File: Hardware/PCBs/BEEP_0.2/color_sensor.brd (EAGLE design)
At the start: 26.2 x 44.7 mm, 19 parts, among them IC2 TCS32X0, IC3 TCS32X0, IC4 TCS32X0

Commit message: continue work on bottom pcbs
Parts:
- flipped JP1 to the bottom
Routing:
- net COLOR_SENSOR_2: track 54.7 -> 52.5 mm
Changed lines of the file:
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@@
 <element name="IC4" library="BEEP" package="TCS32X0" value="TCS32X0" x="13.97" y="16.51" rot="R180"/>
 <element name="C3" library="rcl" package="C0805" value="100n" x="8.9662" y="16.7386" rot="R270"/>
-<element name="JP1" library="pinhead" package="1X09" value="" x="23.0378" y="26.162" rot="R270"/>
+<element name="JP1" library="pinhead" package="1X09" value="" x="23.0378" y="26.162" rot="MR270"/>
 <element name="R1" library="rcl" package="M0805" value="" x="15.1638" y="7.2898" rot="R180"/>
 <element name="LED1" library="led" package="NFSG036BT" value="NFSG036BT" x="21.7424" y="7.9756" rot="R270"/>
@@
 <wire x1="9.5758" y1="42.5704" x2="9.5758" y2="45.1358" width="0.2032" layer="16"/>
 <via x="9.5758" y="45.1358" extent="1-16" drill="0.75" shape="octagon"/>
-<wire x1="23.0378" y1="36.322" x2="21.3614" y2="36.2712" width="0.2032" layer="1"/>
-<wire x1="21.3614" y1="36.2712" x2="17.2466" y2="40.386" width="0.2032" layer="1"/>
 <wire x1="17.2466" y1="40.386" x2="17.2466" y2="43.7134" width="0.2032" layer="1"/>
 <wire x1="17.2466" y1="43.7134" x2="15.7988" y2="45.1612" width="0.2032" layer="1"/>
@@
 <wire x1="6.604" y1="43.434" x2="4.6698" y2="43.434" width="0.2032" layer="1"/>
 <wire x1="4.6698" y1="43.434" x2="4.6482" y2="43.4556" width="0.2032" layer="1"/>
+<wire x1="23.0378" y1="36.322" x2="21.3106" y2="36.322" width="0.2032" layer="1"/>
+<wire x1="21.3106" y1="36.322" x2="17.2466" y2="40.386" width="0.2032" layer="1"/>
 <wire x1="9.2964" y1="29.8044" x2="10.011" y2="29.63" width="0" layer="19" extent="1-1"/>
 </signal>
@@
 <wire x1="12.1158" y1="38.3794" x2="12.1158" y2="37.0958" width="0.2032" layer="1"/>
 <wire x1="12.1158" y1="37.0958" x2="12.065" y2="37.045" width="0.2032" layer="1"/>
-<wire x1="23.0378" y1="33.782" x2="22.3012" y2="33.7312" width="0.2032" layer="1"/>
-<wire x1="22.3012" y1="33.7312" x2="15.9004" y2="40.132" width="0.2032" layer="1"/>
 <wire x1="15.9004" y1="40.132" x2="15.9004" y2="41.6696" width="0.2032" layer="1"/>
 <wire x1="15.9004" y1="41.6696" x2="15.875" y2="41.695" width="0.2032" layer="1"/>
 <wire x1="9.2964" y1="27.9044" x2="9.2964" y2="27.7486" width="0.2032" layer="1"/>
 <wire x1="9.2964" y1="27.7486" x2="12.065" y2="24.98" width="0.2032" layer="1"/>
+<wire x1="23.0378" y1="33.782" x2="22.2504" y2="33.782" width="0.2032" layer="1"/>
+<wire x1="22.2504" y1="33.782" x2="15.9004" y2="40.132" width="0.2032" layer="1"/>
 </signal>
 <signal name="COLOR_SENSOR_PWM_LED">
@@
 <contactref element="R2" pad="2"/>
 <contactref element="R3" pad="2"/>
-<wire x1="25.146" y1="32.131" x2="24.257" y2="31.242" width="0.2032" layer="1"/>
-<wire x1="24.257" y1="31.242" x2="23.0378" y2="31.242" width="0.2032" layer="1"/>
+<wire x1="25.146" y1="32.131" x2="24.511" y2="31.496" width="0.2032" layer="1"/>
 <wire x1="3.9624" y1="39.6596" x2="3.2106" y2="39.6596" width="0.2032" layer="1"/>
 <wire x1="3.2106" y1="39.6596" x2="2.54" y2="38.989" width="0.2032" layer="1"/>
@@
 <wire x1="12.954" y1="48.133" x2="2.794" y2="48.133" width="0.2032" layer="1"/>
 <wire x1="2.794" y1="48.133" x2="2.159" y2="47.498" width="0.2032" layer="1"/>
+<wire x1="23.0378" y1="31.242" x2="24.257" y2="31.242" width="0.2032" layer="1"/>
+<wire x1="24.257" y1="31.242" x2="24.511" y2="31.496" width="0.2032" layer="1"/>
 </signal>
 <signal name="COLOR_SENSOR_1">
@@
 <wire x1="2.921" y1="8.509" x2="3.429" y2="8.001" width="0.2032" layer="1"/>
 <wire x1="3.429" y1="8.001" x2="9.3472" y2="8.001" width="0.2032" layer="1"/>
-<wire x1="23.0378" y1="16.002" x2="23.0378" y2="11.7602" width="0.2032" layer="1"/>
 <wire x1="23.0378" y1="11.7602" x2="24.257" y2="10.541" width="0.2032" layer="1"/>
 <wire x1="24.257" y1="10.541" x2="24.257" y2="8.382" width="0.2032" layer="1"/>
@@
 <wire x1="18.923" y1="8.001" x2="18.288" y2="8.636" width="0.2032" layer="1"/>
 <wire x1="18.288" y1="8.636" x2="9.9822" y2="8.636" width="0.2032" layer="1"/>
+<wire x1="23.0378" y1="11.7602" x2="23.0378" y2="16.002" width="0.2032" layer="1"/>
 </signal>
 <signal name="COLOR_DIODE_1">
@@
 <wire x1="18.3134" y1="18.5928" x2="18.3134" y2="23.0886" width="0.2032" layer="16"/>
 <contactref element="JP1" pad="5"/>
-<wire x1="23.0378" y1="26.162" x2="20.9804" y2="26.1112" width="0.2032" layer="1"/>
-<wire x1="20.9804" y1="26.1112" x2="20.193" y2="26.8986" width="0.2032" layer="1"/>
 <wire x1="20.193" y1="26.8986" x2="20.193" y2="32.4104" width="0.2032" layer="1"/>
 <wire x1="20.193" y1="32.4104" x2="18.288" y2="34.3154" width="0.2032" layer="1"/>
+<wire x1="23.0378" y1="26.162" x2="20.9296" y2="26.162" width="0.2032" layer="1"/>
+<wire x1="20.9296" y1="26.162" x2="20.193" y2="26.8986" width="0.2032" layer="1"/>
 </signal>
 <signal name="COLOR_SENSOR_3">
@@
 <contactref element="JP1" pad="7"/>
 <wire x1="20.1676" y1="12.3444" x2="20.1676" y2="18.7452" width="0.2032" layer="1"/>
-<wire x1="20.1676" y1="18.7452" x2="22.4536" y2="21.0312" width="0.2032" layer="1"/>
-<wire x1="22.4536" y1="21.0312" x2="23.0378" y2="21.082" width="0.2032" layer="1"/>
 <wire x1="7.3914" y1="13.589" x2="7.3914" y2="18.8214" width="0.2032" layer="1"/>
 <wire x1="7.3914" y1="18.8214" x2="9.525" y2="20.955" width="0.2032" layer="1"/>
 <wire x1="9.525" y1="20.955" x2="12.3952" y2="20.955" width="0.2032" layer="1"/>
+<wire x1="23.0378" y1="21.082" x2="22.5044" y2="21.082" width="0.2032" layer="1"/>
+<wire x1="22.5044" y1="21.082" x2="20.1676" y2="18.7452" width="0.2032" layer="1"/>
 </signal>
 <signal name="COLOR_SENSOR_2">
@@
 <wire x1="19.1008" y1="10.16" x2="20.955" y2="12.0142" width="0.2032" layer="1"/>
 <wire x1="20.955" y1="12.0142" x2="20.955" y2="16.9926" width="0.2032" layer="1"/>
-<wire x1="20.955" y1="16.9926" x2="22.4028" y2="18.4404" width="0.2032" layer="1"/>
-<wire x1="22.4028" y1="18.4404" x2="24.1808" y2="18.4404" width="0.2032" layer="1"/>
-<wire x1="24.1808" y1="18.4404" x2="23.0378" y2="18.542" width="0.2032" layer="1"/>
 <wire x1="6.5532" y1="13.3096" x2="6.5532" y2="19.1262" width="0.2032" layer="1"/>
 <wire x1="6.5532" y1="19.1262" x2="8.89" y2="21.463" width="0.2032" layer="1"/>
@@
 <wire x1="11.557" y1="32.7914" x2="9.3726" y2="32.7914" width="0.2032" layer="1"/>
 <wire x1="9.3726" y1="32.7914" x2="6.985" y2="30.4038" width="0.2032" layer="1"/>
+<wire x1="23.0378" y1="18.542" x2="22.5044" y2="18.542" width="0.2032" layer="1"/>
+<wire x1="22.5044" y1="18.542" x2="20.955" y2="16.9926" width="0.2032" layer="1"/>
 </signal>
 <signal name="COLOR_FREQ_OUT">
@@
 <wire x1="18.288" y1="11.5824" x2="19.3548" y2="12.6492" width="0.2032" layer="1"/>
 <contactref element="JP1" pad="6"/>
-<wire x1="23.0378" y1="23.622" x2="21.8948" y2="23.622" width="0.2032" layer="1"/>
 <wire x1="21.8948" y1="23.622" x2="19.3548" y2="21.082" width="0.2032" layer="1"/>
 <wire x1="13.462" y1="23.495" x2="15.24" y2="21.717" width="0.2032" layer="1"/>
 <wire x1="15.24" y1="21.717" x2="18.8468" y2="21.717" width="0.2032" layer="1"/>
 <wire x1="18.8468" y1="21.717" x2="19.3548" y2="21.209" width="0.2032" layer="1"/>
+<wire x1="23.0378" y1="23.622" x2="21.8948" y2="23.622" width="0.2032" layer="1"/>
 </signal>
 <signal name="COLOR_DIODE_2">
@@
 <wire x1="16.7386" y1="24.2824" x2="17.1704" y2="24.7142" width="0.2032" layer="1"/>
 <contactref element="JP1" pad="4"/>
-<wire x1="23.0378" y1="28.702" x2="21.463" y2="28.6512" width="0.2032" layer="1"/>
-<wire x1="21.463" y1="28.6512" x2="20.8026" y2="29.3116" width="0.2032" layer="1"/>
 <wire x1="20.8026" y1="29.3116" x2="20.8026" y2="33.274" width="0.2032" layer="1"/>
 <wire x1="20.8026" y1="33.274" x2="18.5166" y2="35.56" width="0.2032" layer="1"/>
 <wire x1="18.5166" y1="35.56" x2="17.1958" y2="35.56" width="0.2032" layer="1"/>
 <wire x1="17.1958" y1="35.56" x2="17.145" y2="35.6108" width="0.2032" layer="1"/>
+<wire x1="23.0378" y1="28.702" x2="21.4122" y2="28.702" width="0.2032" layer="1"/>
+<wire x1="21.4122" y1="28.702" x2="20.8026" y2="29.3116" width="0.2032" layer="1"/>
 </signal>
 <signal name="N$1">

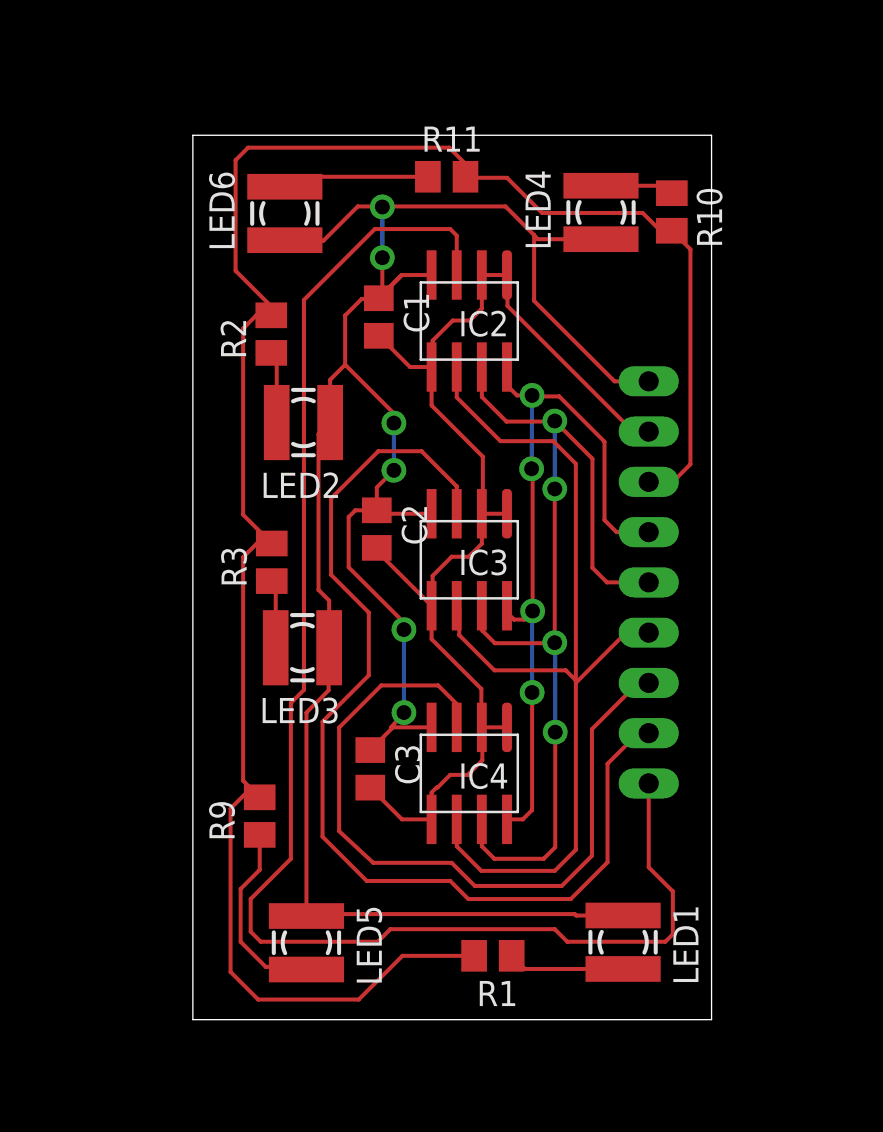
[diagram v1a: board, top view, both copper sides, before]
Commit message: the forgotten commit ;)
* enhance bottom, rgb sensor pcb
* create attiny and lm239 eval boards
* bug fix for the pdf export scripts
* correct attiny soft power switch simulation
* add experimental color sensor code
* add rgb color look up table
* correct motor roations
* various other (this is the forgetten commit)
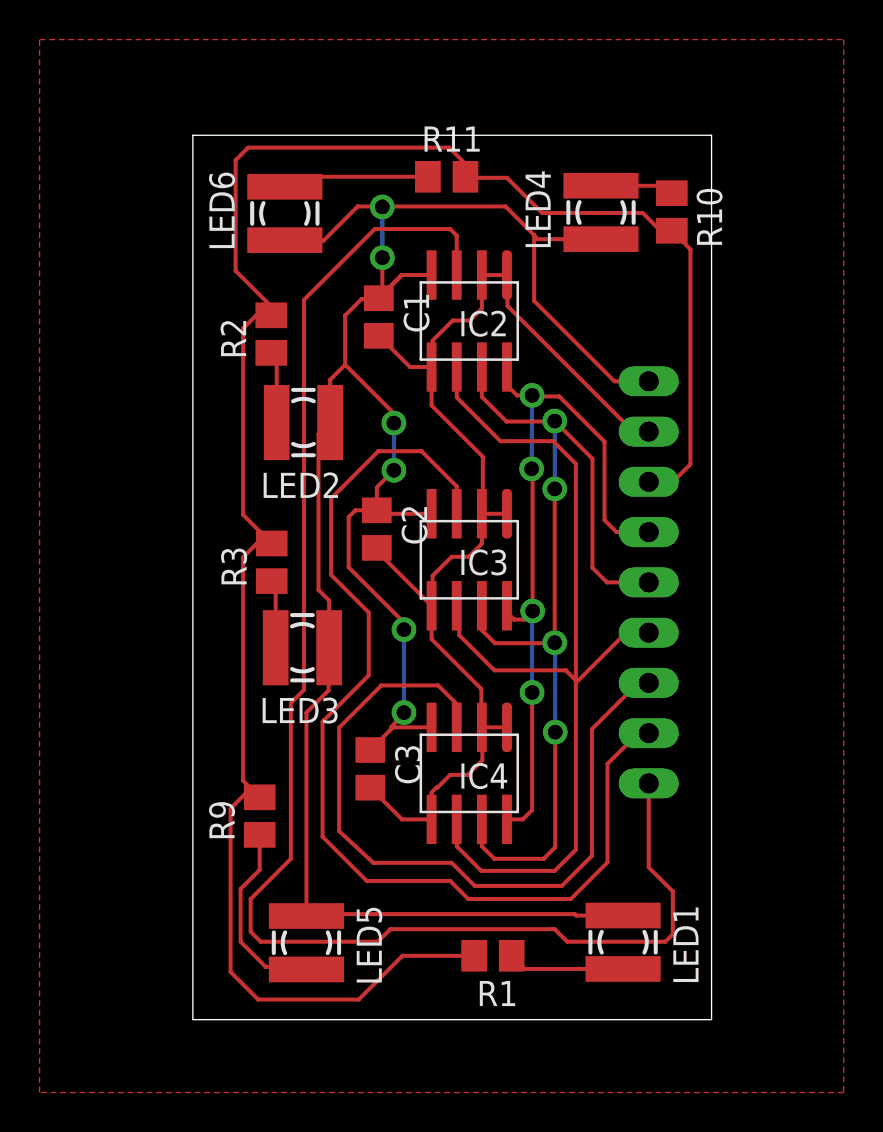
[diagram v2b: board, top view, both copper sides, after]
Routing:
- added copper zone on layer 1, net GND
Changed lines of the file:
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@@
 <layer number="43" name="vRestrict" color="2" fill="10" visible="yes" active="yes"/>
 <layer number="44" name="Drills" color="7" fill="1" visible="no" active="yes"/>
-<layer number="45" name="Holes" color="7" fill="1" visible="no" active="yes"/>
+<layer number="45" name="Holes" color="7" fill="1" visible="yes" active="yes"/>
 <layer number="46" name="Milling" color="3" fill="1" visible="no" active="yes"/>
 <layer number="47" name="Measures" color="7" fill="1" visible="no" active="yes"/>
-<layer number="48" name="Document" color="7" fill="1" visible="yes" active="yes"/>
-<layer number="49" name="Reference" color="7" fill="1" visible="yes" active="yes"/>
+<layer number="48" name="Document" color="7" fill="1" visible="no" active="yes"/>
+<layer number="49" name="Reference" color="7" fill="1" visible="no" active="yes"/>
 <layer number="51" name="tDocu" color="7" fill="1" visible="yes" active="yes"/>
 <layer number="52" name="bDocu" color="7" fill="1" visible="yes" active="yes"/>
@@
 <wire x1="23.0378" y1="36.322" x2="21.3106" y2="36.322" width="0.2032" layer="1"/>
 <wire x1="21.3106" y1="36.322" x2="17.2466" y2="40.386" width="0.2032" layer="1"/>
-<wire x1="9.2964" y1="29.8044" x2="10.011" y2="29.63" width="0" layer="19" extent="1-1"/>
+<polygon width="0.4064" layer="1" isolate="0.3048">
+<vertex x="-7.747" y="53.594"/>
+<vertex x="32.893" y="53.594"/>
+<vertex x="32.893" y="0.381"/>
+<vertex x="-7.747" y="0.381"/>
+</polygon>
 </signal>
 <signal name="N$17">
